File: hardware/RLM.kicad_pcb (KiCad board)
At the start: 2 copper layers, 79.4 x 61 mm, 28 parts, among them U3 AP1117-33, U7 MCP2562-E-SN

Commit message: feat: layout v2
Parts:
- H1, H2, H3, H4: footprint MountingHole:MountingHole_4.3mm_M4 -> MountingHole:MountingHole_4.3mm_M4_ISO14580_Pad
- moved R1 123.2 mm to (181.0, 47.0)
- moved D1 123.1 mm to (183.5, 47.0)
- moved C1 120.6 mm to (178.4, 52.2)
- moved C2 120.6 mm to (181.0, 52.2)
- moved C3 120.6 mm to (183.5, 52.2)
- moved U3 120.6 mm to (181.0, 40.0)
- moved C4 117.3 mm to (178.4, 47.0)
- moved R2 117.0 mm to (183.5, 69.2), turned to 90 degrees
- moved C6 114.2 mm to (181.0, 69.2), turned to 90 degrees
- moved C5 111.3 mm to (178.4, 69.2), turned to 90 degrees
- moved U7 104.3 mm to (181.0, 62.9), turned to 90 degrees
- moved R3 56.0 mm to (103.3, 45.1), turned to 180 degrees
- moved R4 45.7 mm to (103.3, 62.2), turned to 180 degrees
- moved CAN 29.8 mm to (165.3, 78.1)
- moved Shield 21.1 mm to (171.4, 69.8), turned to 0 degrees
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- renumbered BN-220 to GPS
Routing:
- net NRF_VCC: track 21.5 -> 0.00 mm
- net GND: track 16.4 -> 0.00 mm
- net +3.3V: track 15.3 -> 0.00 mm
- net Net-(D1-K): track 5.11 -> 0.00 mm
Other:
- board size 79.4 x 61 mm -> 88.9 x 59.1 mm
- board text added: "Remote Logging Module V1 By: Evan Rutten"
- board text removed: "GRC RLM V1 By: Evan R."

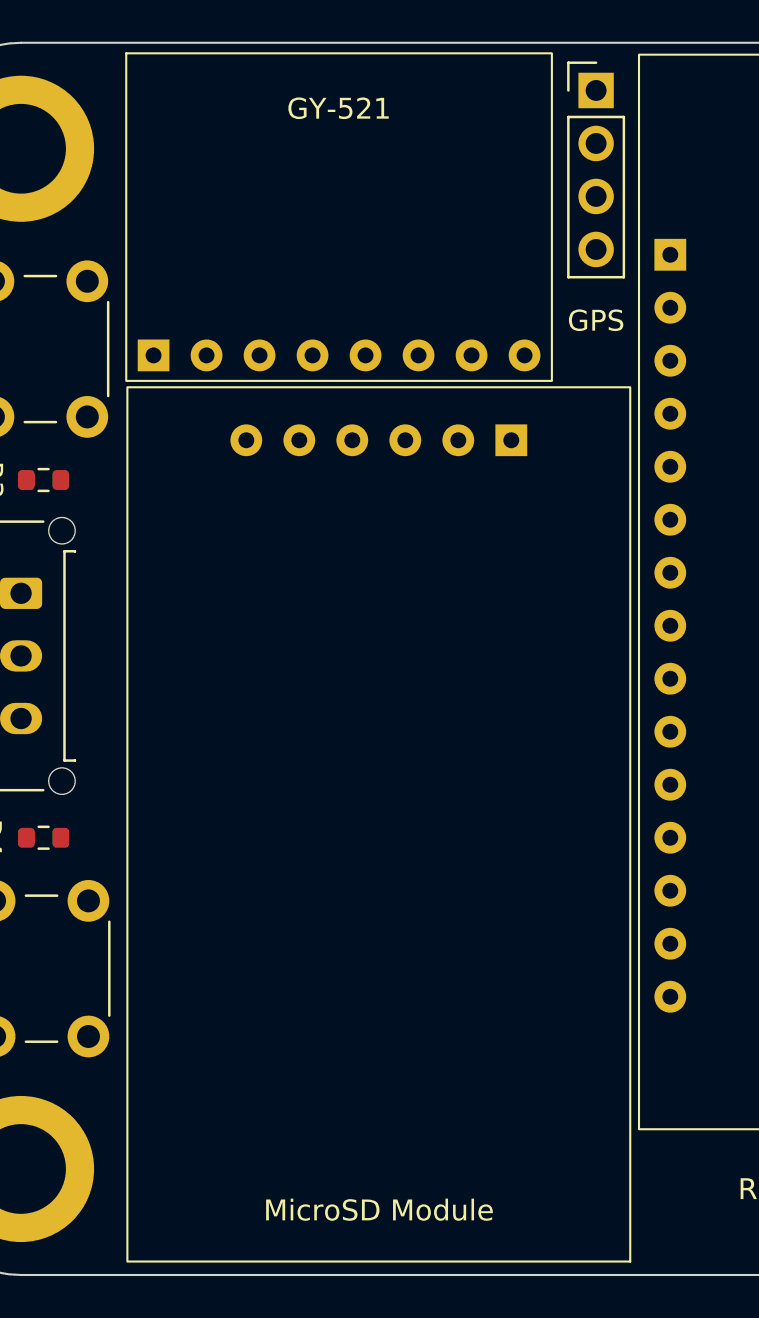
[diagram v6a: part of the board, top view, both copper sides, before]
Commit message: feat: move all ports to the same side
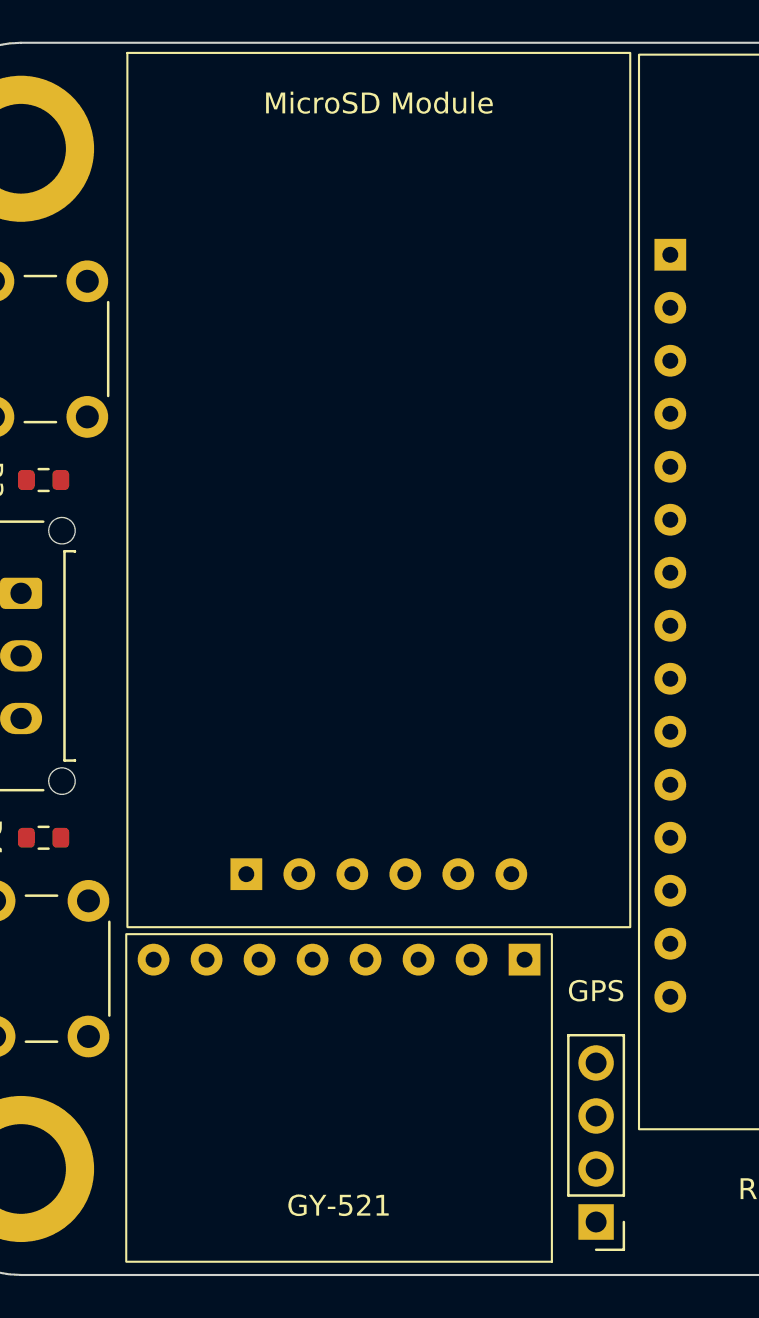
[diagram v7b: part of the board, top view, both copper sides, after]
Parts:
- moved MicroSD Module 57.9 mm to (119.4, 24.6), turned to 0 degrees
- moved GY-521 57.9 mm to (117.5, 82.5), turned to 180 degrees
- moved GPS 54.2 mm to (129.8, 80.6), turned to 180 degrees
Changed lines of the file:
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@@
   )
   (footprint "GRC:MicroSD-Module" (layer "F.Cu")
-    (at 119.38 82.54 180)
+    (at 119.38 24.616)
     (property "Sheetfile" "RLM.kicad_sch")
     (property "Sheetname" "")
@@
         (effects (font (size 1 1) (thickness 0.1)))
     )
-    (fp_text value "~" (at 0 5.08 180 unlocked) (layer "F.Fab") hide
+    (fp_text value "~" (at 0 5.08 unlocked) (layer "F.Fab") hide
         (effects (font (size 1 1) (thickness 0.15)))
     )
@@
     (fp_rect (start -12.05 0) (end 12.05 41.9)
       (stroke (width 0.1) (type default)) (fill none) (layer "F.SilkS"))
-    (pad "1" thru_hole rect (at -6.35 39.36 180) (size 1.524 1.524) (drill 0.762) (layers "*.Cu" "*.Mask")
+    (pad "1" thru_hole rect (at -6.35 39.36) (size 1.524 1.524) (drill 0.762) (layers "*.Cu" "*.Mask")
       (net 1 "GND") (pinfunction "GND") (pintype "bidirectional"))
-    (pad "2" thru_hole circle (at -3.81 39.36 180) (size 1.524 1.524) (drill 0.762) (layers "*.Cu" "*.Mask")
+    (pad "2" thru_hole circle (at -3.81 39.36) (size 1.524 1.524) (drill 0.762) (layers "*.Cu" "*.Mask")
       (net 24 "+5V") (pinfunction "VCC") (pintype "bidirectional"))
-    (pad "3" thru_hole circle (at -1.27 39.36 180) (size 1.524 1.524) (drill 0.762) (layers "*.Cu" "*.Mask")
+    (pad "3" thru_hole circle (at -1.27 39.36) (size 1.524 1.524) (drill 0.762) (layers "*.Cu" "*.Mask")
       (net 33 "SPI_MISO") (pinfunction "MISO") (pintype "bidirectional"))
-    (pad "4" thru_hole circle (at 1.27 39.36 180) (size 1.524 1.524) (drill 0.762) (layers "*.Cu" "*.Mask")
+    (pad "4" thru_hole circle (at 1.27 39.36) (size 1.524 1.524) (drill 0.762) (layers "*.Cu" "*.Mask")
       (net 36 "SPI_MOSI") (pinfunction "MOSI") (pintype "bidirectional"))
-    (pad "5" thru_hole circle (at 3.81 39.36 180) (size 1.524 1.524) (drill 0.762) (layers "*.Cu" "*.Mask")
+    (pad "5" thru_hole circle (at 3.81 39.36) (size 1.524 1.524) (drill 0.762) (layers "*.Cu" "*.Mask")
       (net 32 "SPI_SCK") (pinfunction "CLK") (pintype "bidirectional"))
-    (pad "6" thru_hole circle (at 6.35 39.36 180) (size 1.524 1.524) (drill 0.762) (layers "*.Cu" "*.Mask")
+    (pad "6" thru_hole circle (at 6.35 39.36) (size 1.524 1.524) (drill 0.762) (layers "*.Cu" "*.Mask")
       (net 39 "SD_CS") (pinfunction "CS") (pintype "bidirectional"))
   )
@@
   )
   (footprint "GRC:GY-521" (layer "F.Cu")
-    (at 117.475 24.635)
+    (at 117.475 82.55 180)
     (property "Sheetfile" "RLM.kicad_sch")
     (property "Sheetname" "")
@@
         (effects (font (size 1 1) (thickness 0.1)))
     )
-    (fp_text value "~" (at 0 3.81 unlocked) (layer "F.Fab") hide
+    (fp_text value "~" (at 0 3.81 180 unlocked) (layer "F.Fab") hide
         (effects (font (size 1 1) (thickness 0.15)))
     )
@@
     (fp_rect (start -10.2 0) (end 10.2 15.7)
       (stroke (width 0.1) (type default)) (fill none) (layer "F.SilkS"))
-    (pad "1" thru_hole rect (at -8.89 14.478) (size 1.524 1.524) (drill 0.762) (layers "*.Cu" "*.Mask")
+    (pad "1" thru_hole rect (at -8.89 14.478 180) (size 1.524 1.524) (drill 0.762) (layers "*.Cu" "*.Mask")
       (net 3 "+3.3V") (pinfunction "VCC") (pintype "bidirectional"))
-    (pad "2" thru_hole circle (at -6.35 14.478) (size 1.524 1.524) (drill 0.762) (layers "*.Cu" "*.Mask")
+    (pad "2" thru_hole circle (at -6.35 14.478 180) (size 1.524 1.524) (drill 0.762) (layers "*.Cu" "*.Mask")
       (net 1 "GND") (pinfunction "GND") (pintype "bidirectional"))
-    (pad "3" thru_hole circle (at -3.81 14.478) (size 1.524 1.524) (drill 0.762) (layers "*.Cu" "*.Mask")
+    (pad "3" thru_hole circle (at -3.81 14.478 180) (size 1.524 1.524) (drill 0.762) (layers "*.Cu" "*.Mask")
       (net 35 "I2C_SCL") (pinfunction "SCL") (pintype "bidirectional"))
-    (pad "4" thru_hole circle (at -1.27 14.478) (size 1.524 1.524) (drill 0.762) (layers "*.Cu" "*.Mask")
+    (pad "4" thru_hole circle (at -1.27 14.478 180) (size 1.524 1.524) (drill 0.762) (layers "*.Cu" "*.Mask")
       (net 34 "I2C_SDA") (pinfunction "SDA") (pintype "bidirectional"))
-    (pad "5" thru_hole circle (at 1.27 14.478) (size 1.524 1.524) (drill 0.762) (layers "*.Cu" "*.Mask")
+    (pad "5" thru_hole circle (at 1.27 14.478 180) (size 1.524 1.524) (drill 0.762) (layers "*.Cu" "*.Mask")
       (net 37 "unconnected-(U4-XDA-Pad5)") (pinfunction "XDA") (pintype "bidirectional+no_connect"))
-    (pad "6" thru_hole circle (at 3.81 14.478) (size 1.524 1.524) (drill 0.762) (layers "*.Cu" "*.Mask")
+    (pad "6" thru_hole circle (at 3.81 14.478 180) (size 1.524 1.524) (drill 0.762) (layers "*.Cu" "*.Mask")
       (net 38 "unconnected-(U4-XCL-Pad6)") (pinfunction "XCL") (pintype "bidirectional+no_connect"))
-    (pad "7" thru_hole circle (at 6.35 14.478) (size 1.524 1.524) (drill 0.762) (layers "*.Cu" "*.Mask")
+    (pad "7" thru_hole circle (at 6.35 14.478 180) (size 1.524 1.524) (drill 0.762) (layers "*.Cu" "*.Mask")
       (net 40 "unconnected-(U4-ADO-Pad7)") (pinfunction "ADO") (pintype "bidirectional+no_connect"))
-    (pad "8" thru_hole circle (at 8.89 14.478) (size 1.524 1.524) (drill 0.762) (layers "*.Cu" "*.Mask")
+    (pad "8" thru_hole circle (at 8.89 14.478 180) (size 1.524 1.524) (drill 0.762) (layers "*.Cu" "*.Mask")
       (net 41 "unconnected-(U4-INT-Pad8)") (pinfunction "INT") (pintype "bidirectional+no_connect"))
   )
@@
   )
   (footprint "Connector_PinHeader_2.54mm:PinHeader_1x04_P2.54mm_Vertical" (layer "F.Cu")
-    (at 129.794 26.416)
+    (at 129.794 80.645 180)
     (descr "Through hole straight pin header, 1x04, 2.54mm pitch, single row")
     (tags "Through hole pin header THT 1x04 2.54mm single row")
@@
     (fp_line (start 1.27 8.89) (end -1.27 8.89)
       (stroke (width 0.1) (type solid)) (layer "F.Fab"))
-    (pad "1" thru_hole rect (at 0 0) (size 1.7 1.7) (drill 1) (layers "*.Cu" "*.Mask")
+    (pad "1" thru_hole rect (at 0 0 180) (size 1.7 1.7) (drill 1) (layers "*.Cu" "*.Mask")
       (net 1 "GND") (pinfunction "GND") (pintype "bidirectional"))
-    (pad "2" thru_hole oval (at 0 2.54) (size 1.7 1.7) (drill 1) (layers "*.Cu" "*.Mask")
+    (pad "2" thru_hole oval (at 0 2.54 180) (size 1.7 1.7) (drill 1) (layers "*.Cu" "*.Mask")
       (net 22 "GPS_TX") (pinfunction "TX") (pintype "bidirectional"))
-    (pad "3" thru_hole oval (at 0 5.08) (size 1.7 1.7) (drill 1) (layers "*.Cu" "*.Mask")
+    (pad "3" thru_hole oval (at 0 5.08 180) (size 1.7 1.7) (drill 1) (layers "*.Cu" "*.Mask")
       (net 23 "GPS_RX") (pinfunction "RX") (pintype "bidirectional"))
-    (pad "4" thru_hole oval (at 0 7.62) (size 1.7 1.7) (drill 1) (layers "*.Cu" "*.Mask")
+    (pad "4" thru_hole oval (at 0 7.62 180) (size 1.7 1.7) (drill 1) (layers "*.Cu" "*.Mask")
       (net 3 "+3.3V") (pinfunction "VCC") (pintype "bidirectional"))
     (model "${KICAD6_3DMODEL_DIR}/Connector_PinHeader_2.54mm.3dshapes/PinHeader_1x04_P2.54mm_Vertical.wrl"

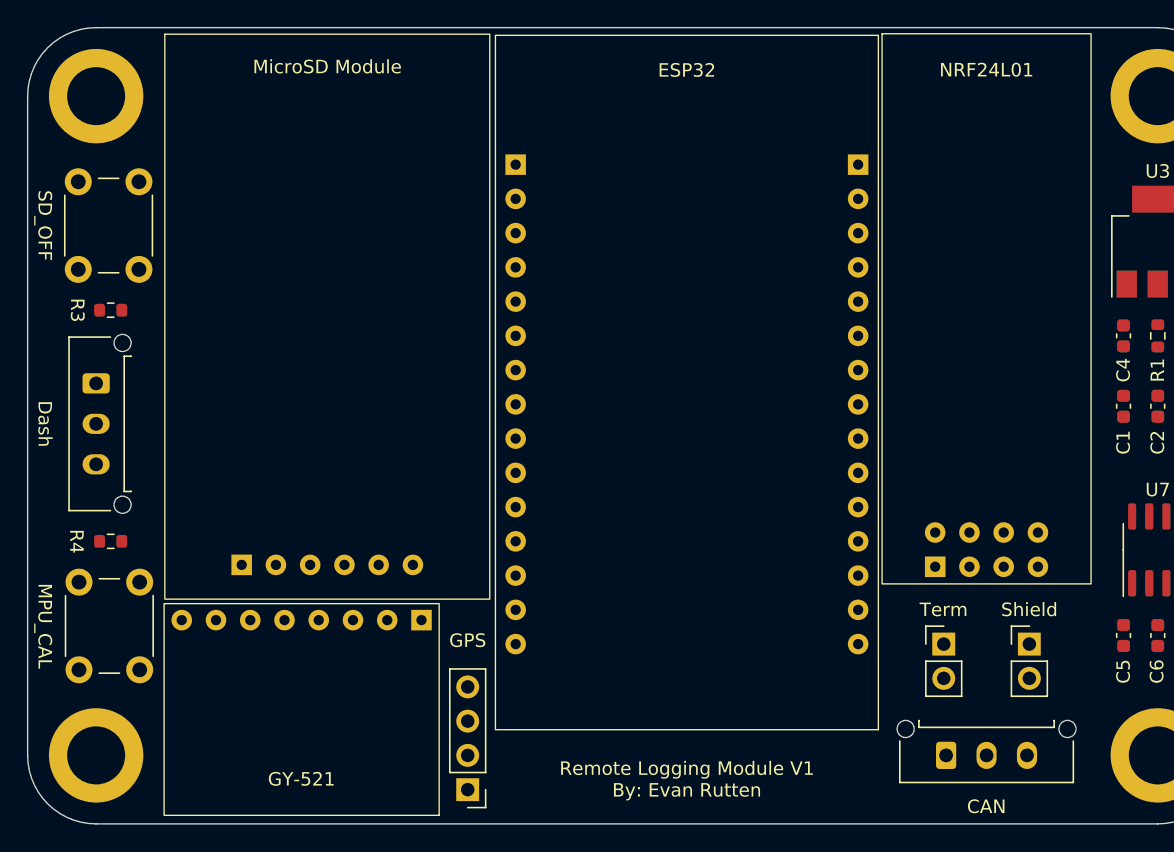
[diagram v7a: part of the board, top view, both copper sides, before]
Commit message: feat: update symbols to have VCC up and GND down
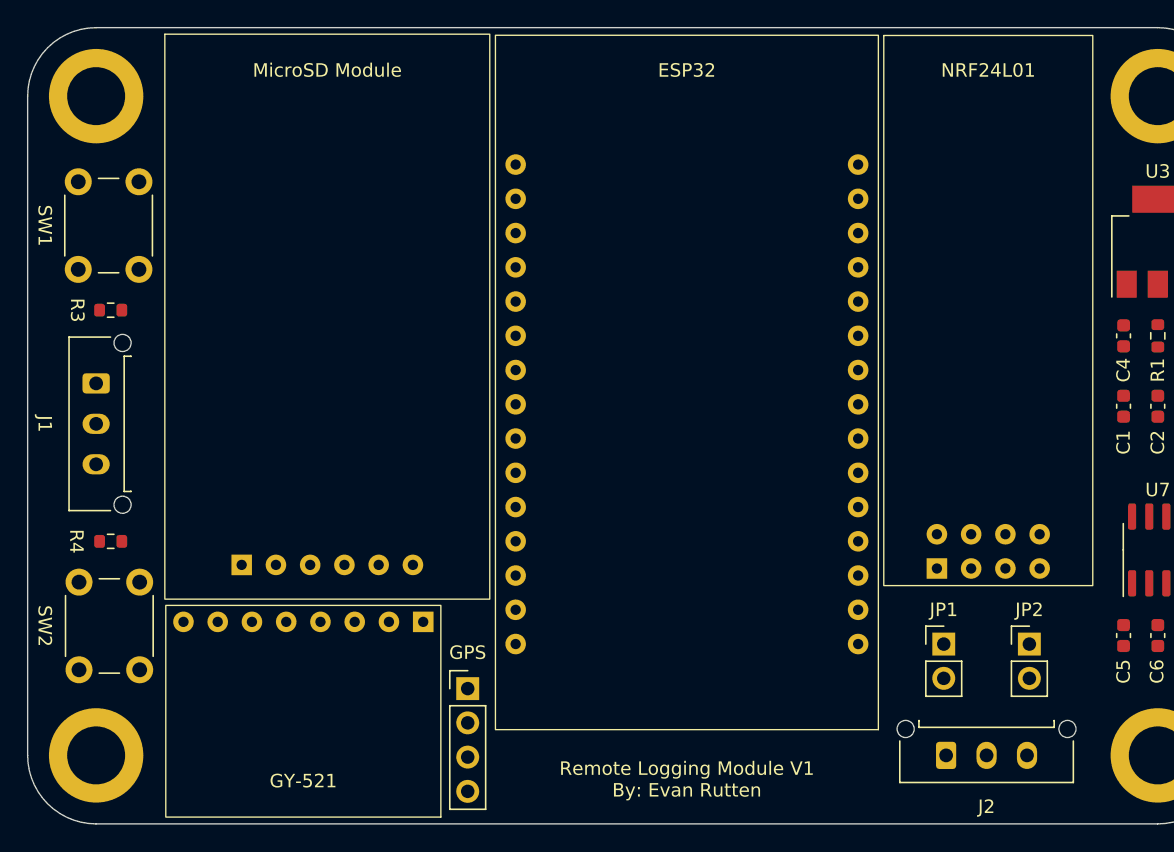
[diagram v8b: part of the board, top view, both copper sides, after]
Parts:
- ESP32: value ~ -> U1
- GPS: value ~ -> U5
- GY-521: value ~ -> U4
- MicroSD Module: value ~ -> U6
- NRF24L01: value ~ -> U2
- moved GPS 7.49 mm to (129.8, 73.2), turned to 0 degrees
- moved GY-521 0.18 mm to (117.6, 82.7)
- moved NRF24L01 0.18 mm to (168.4, 65.5)
- renumbered Dash to J1, CAN to J2, Term to JP1, Shield to JP2, SD_OFF to SW1, MPU_CAL to SW2
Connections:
- C1 pad 1: +3.3V -> +5V
- C2 pad 1: +3.3V -> +5V
- GPS pad 4: +3.3V -> +5V
- J1 pad 1: +5V -> GND
- J1 pad 2: GND -> V_SENSE
- J1 pad 3: V_SENSE -> +5V
- U3 pad 3: +3.3V -> +5V
